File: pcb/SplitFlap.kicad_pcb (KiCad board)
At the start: 2 copper layers, 35 x 35 mm, 20 parts, among them U1 PCF8575DBR, U2 ULN2003

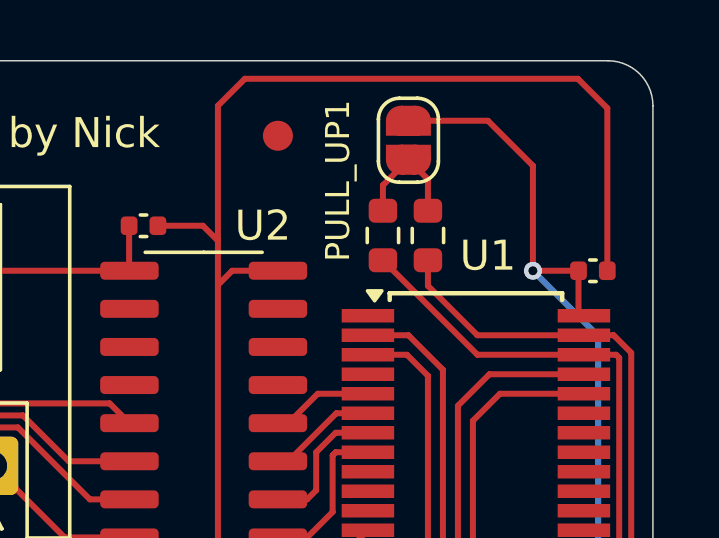
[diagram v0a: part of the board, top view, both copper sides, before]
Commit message: Remove data line pull-ups
The SCL and SDL pull-ups need to happen on 3.3v, yet in the current
design they are attached to the 5v line.  Since they are only necessary
once per circuit (8 boards + esp32) I will leave them out of the board
design.
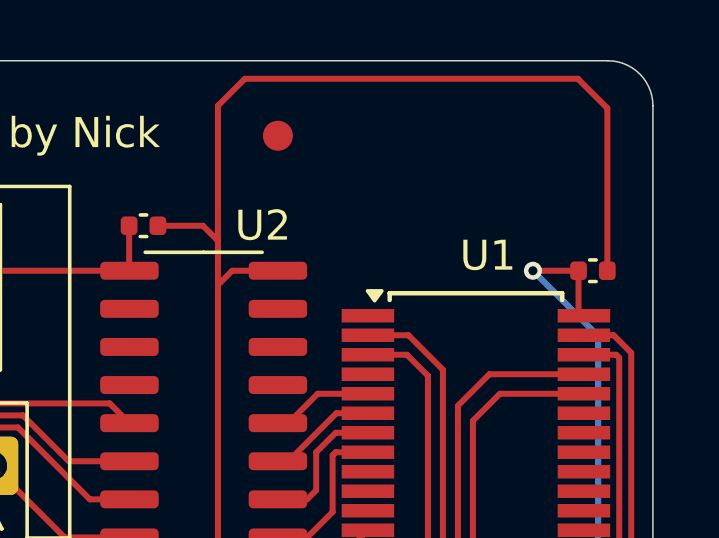
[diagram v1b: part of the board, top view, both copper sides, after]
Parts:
- removed PULL_UP1: SolderJumper_2_Open, Jumper:SolderJumper-2_P1.3mm_Open_RoundedPad1.0x1.5mm
- removed PULL_UP3, PULL_UP4: 10K, Resistor_SMD:R_0603_1608Metric
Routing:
- net +5V: track 105.2 -> 97.0 mm
- net Net-(NEXT1-Pin_3): track 53.7 -> 45.7 mm
- net Net-(NEXT1-Pin_4): track 54.1 -> 47.4 mm
- net Net-(PULL_UP1-B): track 4.02 -> 0.00 mm

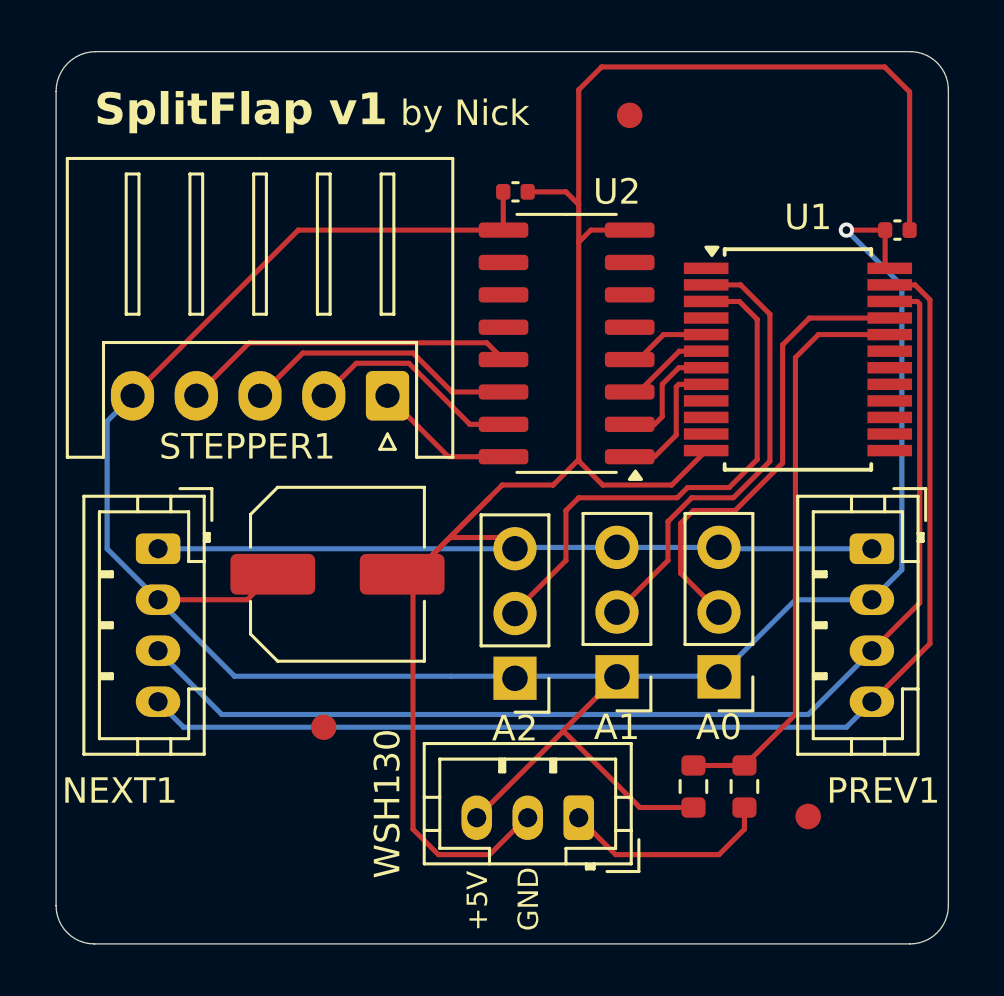
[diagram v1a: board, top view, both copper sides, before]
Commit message: Make space for stepper connector
Moves all components down to increase the space for the stepper motor
JST conector.
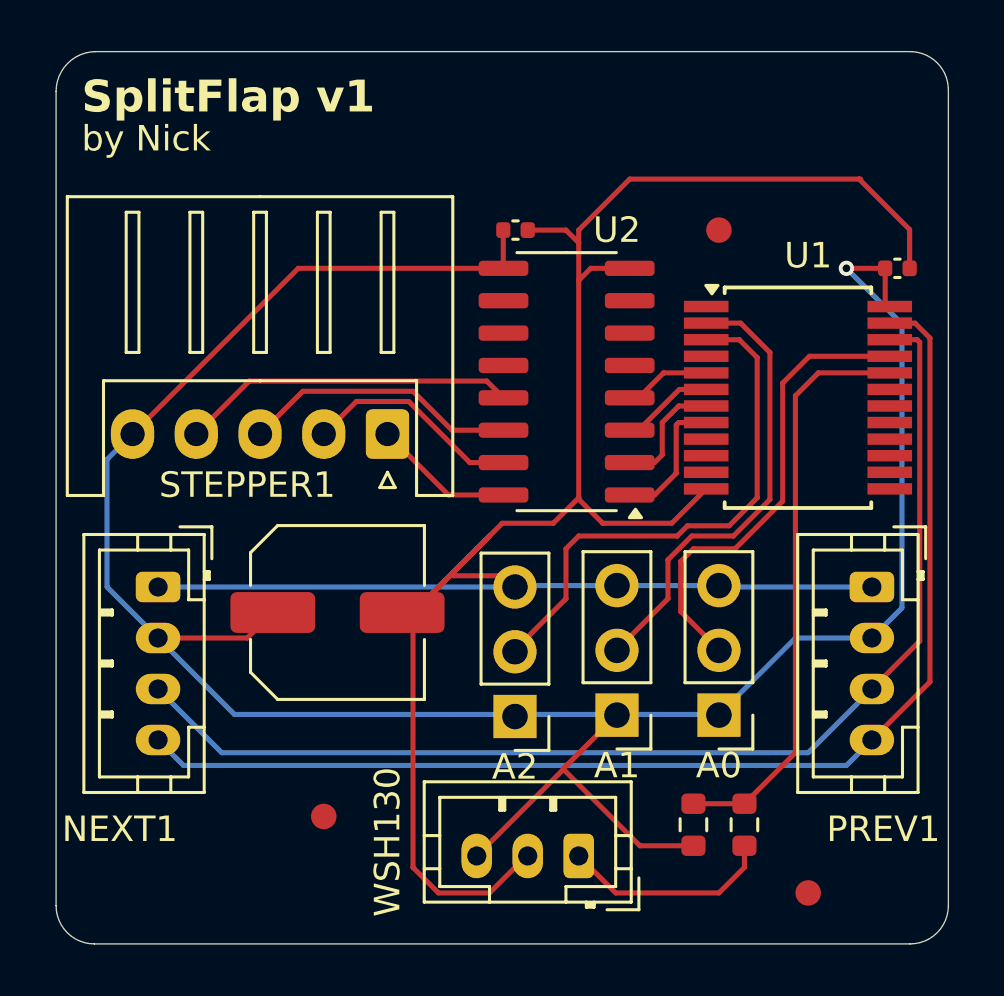
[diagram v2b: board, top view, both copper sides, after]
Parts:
- moved REF** 5.70 mm to (171.0, 66.5)
- moved REF** 3.50 mm to (155.5, 89.5)
- moved REF** 3.00 mm to (174.5, 92.5)
- moved A0 1.50 mm to (171.0, 85.5)
- moved A1 1.50 mm to (167.0, 85.5)
- moved A2 1.50 mm to (163.0, 85.6)
- moved C1 1.50 mm to (178.0, 68.0)
- moved C2_BYPASS1 1.50 mm to (163.0, 66.5)
- moved C3_BULK1 1.50 mm to (156.0, 81.5)
- moved NEXT1 1.50 mm to (149.0, 80.5)
- moved PREV1 1.50 mm to (177.0, 80.5)
- moved PULL_UP2 1.50 mm to (170.0, 89.8)
- moved SERIES1 1.50 mm to (172.0, 89.8)
- moved STEPPER1 1.50 mm to (158.0, 74.5)
- moved U1 1.50 mm to (174.1, 73.1)
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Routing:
- net GND: track 104.1 -> 97.2 mm

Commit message: Re-route U1 bypass capacitor
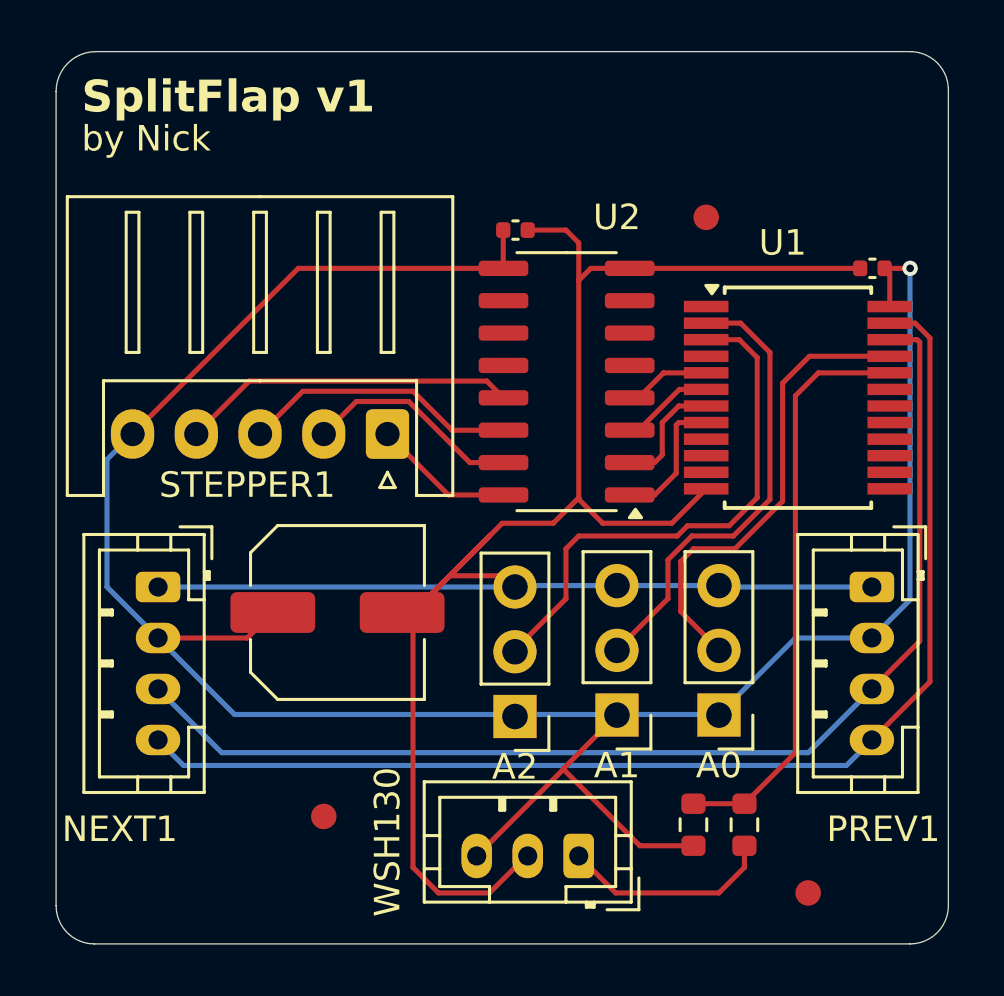
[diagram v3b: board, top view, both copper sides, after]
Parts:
- moved C1 0.98 mm to (177.0, 68.0), turned to 180 degrees
- moved REF** 0.71 mm to (170.5, 66.0)
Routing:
- net GND: track 97.2 -> 89.5 mm
- net +5V: track 97.0 -> 95.5 mm
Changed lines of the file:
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@@
 		(tags "SSOP 0.65")
 		(property "Reference" "U1"
-			(at 0.4 -5.575 0)
+			(at -0.6 -6.075 0)
 			(layer "F.SilkS")
 			(effects
@@
 		(tags "SOIC SO")
 		(property "Reference" "U2"
-			(at -1.975 5.945 0)
+			(at -1.975 6.445 0)
 			(layer "F.SilkS")
 			(effects
@@
 		(locked yes)
 		(layer "F.Cu")
-		(at 171 66.5)
+		(at 170.5 66)
 		(descr "Circular Fiducial, 1mm bare copper, 2mm soldermask opening (Level A)")
 		(tags "fiducial")
@@
 	(footprint "Capacitor_SMD:C_0402_1005Metric"
 		(layer "F.Cu")
-		(at 178 68)
+		(at 177.02 68 180)
 		(descr "Capacitor SMD 0402 (1005 Metric), square (rectangular) end terminal, IPC_7351 nominal, (Body size source: IPC-SM-782 page 76, https://www.pcb-3d.com/wordpress/wp-content/uploads/ipc-sm-782a_amendment_1_and_2.pdf), generated with kicad-footprint-generator")
 		(tags "capacitor")
@@
 		)
 		(property "Datasheet" ""
-			(at 0 0 0)
+			(at 0 0 180)
 			(unlocked yes)
 			(layer "F.Fab")
@@
 		)
 		(property "Description" "Bypass capacitor, keeps the voltage stable during power-on"
-			(at 0 0 0)
+			(at 0 0 180)
 			(unlocked yes)
 			(layer "F.Fab")
@@
 		)
 		(property "MPN" "C6955083"
-			(at 0 0 0)
+			(at 0 0 180)
 			(unlocked yes)
 			(layer "F.Fab")
@@
 		(attr smd)
 		(fp_line
-			(start -0.107836 -0.36)
-			(end 0.107836 -0.36)
+			(start -0.107836 0.36)
+			(end 0.107836 0.36)
 			(stroke
 				(width 0.12)
@@
 		)
 		(fp_line
-			(start -0.107836 0.36)
-			(end 0.107836 0.36)
+			(start -0.107836 -0.36)
+			(end 0.107836 -0.36)
 			(stroke
 				(width 0.12)
@@
 		)
 		(fp_line
-			(start -0.91 -0.46)
-			(end 0.91 -0.46)
+			(start 0.91 0.46)
+			(end -0.91 0.46)
 			(stroke
 				(width 0.05)
@@
 		)
 		(fp_line
-			(start -0.91 0.46)
-			(end -0.91 -0.46)
+			(start 0.91 -0.46)
+			(end 0.91 0.46)
 			(stroke
 				(width 0.05)
@@
 		)
 		(fp_line
-			(start 0.91 -0.46)
-			(end 0.91 0.46)
+			(start -0.91 0.46)
+			(end -0.91 -0.46)
 			(stroke
 				(width 0.05)
@@
 		)
 		(fp_line
-			(start 0.91 0.46)
-			(end -0.91 0.46)
+			(start -0.91 -0.46)
+			(end 0.91 -0.46)
 			(stroke
 				(width 0.05)
@@
 		)
 		(fp_line
-			(start -0.5 -0.25)
-			(end 0.5 -0.25)
+			(start 0.5 0.25)
+			(end -0.5 0.25)
 			(stroke
 				(width 0.1)
@@
 		)
 		(fp_line
-			(start -0.5 0.25)
-			(end -0.5 -0.25)
+			(start 0.5 -0.25)
+			(end 0.5 0.25)
 			(stroke
 				(width 0.1)
@@
 		)
 		(fp_line
-			(start 0.5 -0.25)
-			(end 0.5 0.25)
+			(start -0.5 0.25)
+			(end -0.5 -0.25)
 			(stroke
 				(width 0.1)
@@
 		)
 		(fp_line
-			(start 0.5 0.25)
-			(end -0.5 0.25)
+			(start -0.5 -0.25)
+			(end 0.5 -0.25)
 			(stroke
 				(width 0.1)
@@
 		)
 		(pad "1" smd roundrect
-			(at -0.48 0)
+			(at -0.48 0 180)
 			(size 0.56 0.62)
 			(layers "F.Cu" "F.Mask" "F.Paste")
@@
 		)
 		(pad "2" smd roundrect
-			(at 0.48 0)
+			(at 0.48 0 180)
 			(size 0.56 0.62)
 			(layers "F.Cu" "F.Mask" "F.Paste")
@@
 	)
 	(segment
-		(start 177.52 68)
-		(end 176 68)
-		(width 0.2)
-		(layer "F.Cu")
-		(net 1)
-	)
-	(segment
 		(start 164.9 87.625)
 		(end 167 85.525)
@@
 	)
 	(segment
-		(start 176 68)
-		(end 176.2 68)
-		(width 0.2)
-		(layer "F.Cu")
-		(net 1)
-	)
-	(segment
-		(start 177.52 69.32)
-		(end 177.7 69.5)
+		(start 177.7 68.2)
+		(end 177.5 68)
 		(width 0.2)
 		(layer "F.Cu")
@@
 	)
 	(segment
-		(start 177.52 68)
-		(end 177.52 69.32)
-		(width 0.2)
-		(layer "F.Cu")
-		(net 1)
-	)
-	(segment
 		(start 178.35 69.5)
 		(end 177.7 69.5)
@@
 	)
 	(segment
+		(start 178.5 68)
+		(end 177.5 68)
+		(width 0.2)
+		(layer "F.Cu")
+		(net 1)
+	)
+	(segment
 		(start 162.54 66.5)
 		(end 162.54 67.99)
@@
 	)
 	(segment
+		(start 177.7 69.5)
+		(end 177.7 68.2)
+		(width 0.2)
+		(layer "F.Cu")
+		(net 1)
+	)
+	(segment
 		(start 154.5 68)
 		(end 148 74.5)
@@
 	)
 	(via
-		(at 176 68)
+		(at 178.5 68)
 		(size 0.6)
 		(drill 0.3)
@@
 	)
 	(segment
-		(start 160.5 85.5)
-		(end 152 85.5)
+		(start 177 82.5)
+		(end 178.5 81)
 		(width 0.2)
 		(layer "B.Cu")
@@
 	)
 	(segment
-		(start 177 82.5)
-		(end 178.176 81.324)
+		(start 160.5 85.5)
+		(end 152 85.5)
 		(width 0.2)
 		(layer "B.Cu")
@@
 	)
 	(segment
-		(start 178.176 70.176)
-		(end 176 68)
-		(width 0.2)
-		(layer "B.Cu")
-		(net 1)
-	)
-	(segment
-		(start 178.176 81.324)
-		(end 178.176 70.176)
-		(width 0.2)
-		(layer "B.Cu")
-		(net 1)
-	)
-	(segment
 		(start 148 74.5)
 		(end 147 75.5)
@@
 	)
 	(segment
+		(start 178.5 81)
+		(end 178.5 68)
+		(width 0.2)
+		(layer "B.Cu")
+		(net 1)
+	)
+	(segment
 		(start 160 92.5)
 		(end 162 92.5)
@@
 	)
 	(segment
-		(start 176.5 64.5)
-		(end 178.48 66.48)
-		(width 0.2)
-		(layer "F.Cu")
-		(net 2)
-	)
-	(segment
 		(start 163.5 66.5)
 		(end 165 66.5)
@@
 	)
 	(segment
-		(start 178.48 66.48)
-		(end 178.48 68)
-		(width 0.2)
-		(layer "F.Cu")
-		(net 2)
-	)
-	(segment
 		(start 165.5 68.475001)
 		(end 165.5 67)
@@
 	)
 	(segment
-		(start 167.5 64.5)
-		(end 165.5 66.5)
-		(width 0.2)
-		(layer "F.Cu")
-		(net 2)
-	)
-	(segment
 		(start 165.5 77.056968)
 		(end 166.443032 78)
@@
 	)
 	(segment
-		(start 165.5 66.5)
-		(end 165.5 67)
-		(width 0.2)
-		(layer "F.Cu")
-		(net 2)
-	)
-	(segment
 		(start 159 91.5)
 		(end 160 92.5)
@@
 	)
 	(segment
-		(start 176.5 64.5)
-		(end 176.561 64.5)
-		(width 0.2)
-		(layer "F.Cu")
-		(net 2)
-	)
-	(segment
 		(start 159 81.5)
 		(end 162 78.5)
@@
 	)
 	(segment
-		(start 167.5 64.5)
-		(end 176.5 64.5)
+		(start 167.5 68)
+		(end 176.54 68)
 		(width 0.2)
 		(layer "F.Cu")
